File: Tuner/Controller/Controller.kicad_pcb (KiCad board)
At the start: 2 copper layers, 96.8 x 99.3 mm, 173 parts, among them J1 Conn_02x05_Odd_Even, J10 Conn_01x05, J11 Conn_01x01, J12 Conn_01x02, J14 Conn_01x01, J15 Conn_01x02, J16 Conn_01x06, J17 Conn_01x01, J18 Conn_01x01, J19 Conn_01x01, J2 Conn_02x05_Odd_Even, J20 Conn_01x01, J21 Conn_01x01, J23 Conn_01x01, J26 Conn_01x02, J27 Conn_01x02, J28 Conn_01x02, J3 Conn_02x05_Odd_Even, J30 Conn_01x02, J4 Conn_02x05_Odd_Even, J5 Conn_02x05_Odd_Even, J7 Conn_01x02, J8 Conn_01x06, Q1 2N3904, Q2 2N3904, Q3 2N3904, Q4 2N3904, Q5 2N3904, Q6 2N3904, Q7 2N3904, Q8 2N3904, U1 74LS393, U2 74HC14, U3 74HC86, U4 LM350_TO220

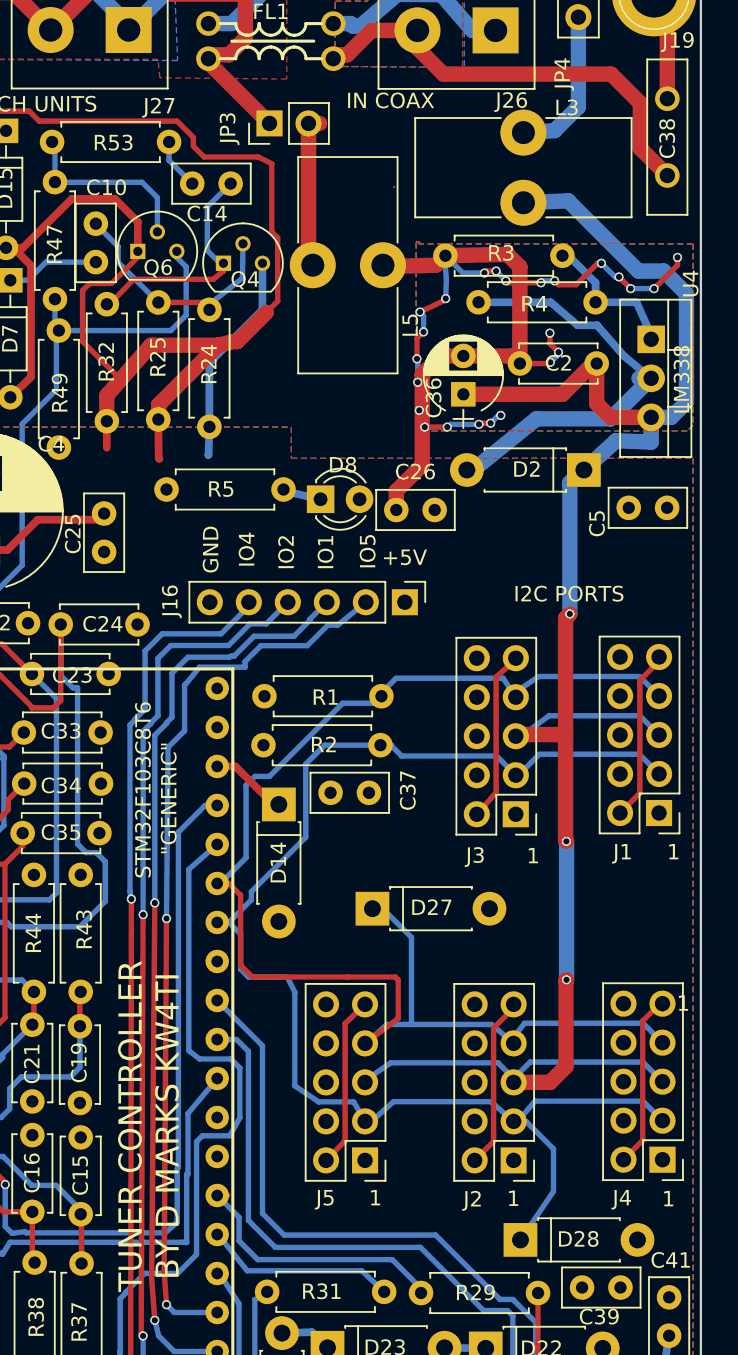
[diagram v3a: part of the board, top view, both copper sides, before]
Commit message: Added HK19F boards
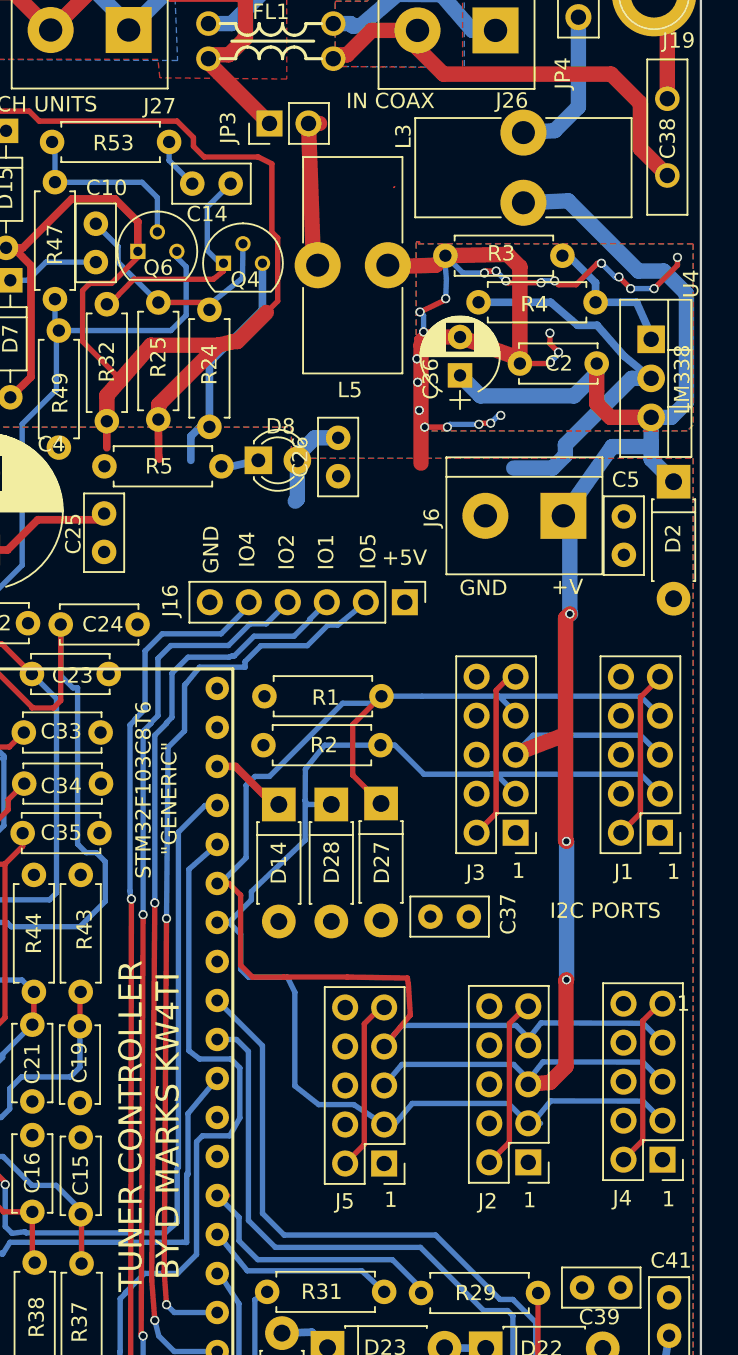
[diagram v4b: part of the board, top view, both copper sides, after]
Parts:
- added J6: Conn_01x02, Connectors_Terminal_Blocks:TerminalBlock_bornier-2_P5.08mm, F.Cu at (143.2, 66.0)
- moved D28 30.9 mm to (128.1, 84.8), turned to 270 degrees
- moved C37 10.4 mm to (137.0, 92.1)
- moved C26 7.85 mm to (128.5, 60.9), turned to 270 degrees
- moved D27 6.87 mm to (131.3, 84.7), turned to 270 degrees
- moved D2 5.89 mm to (150.4, 63.8), turned to 270 degrees
- moved D8 4.78 mm to (123.3, 62.4)
- moved R5 4.32 mm to (120.9, 62.8)
- moved C5 3.08 mm to (147.1, 68.5), turned to 90 degrees
- moved J1 1.29 mm to (149.5, 86.6)
- moved J5 1.26 mm to (131.5, 108.2)
- moved C36 1.25 mm to (136.5, 56.8)
- moved J3 1.21 mm to (140.1, 86.6)
- moved J2 0.96 mm to (140.9, 108.1)
- moved L5 0.32 mm to (127.2, 49.7)
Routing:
- net +5V: track 193.8 -> 199.7 mm
- net I2CSCL: track 91.9 -> 87.5 mm
- net UPWR: track 124.0 -> 127.7 mm
- net GND: track 622.4 -> 620.3 mm

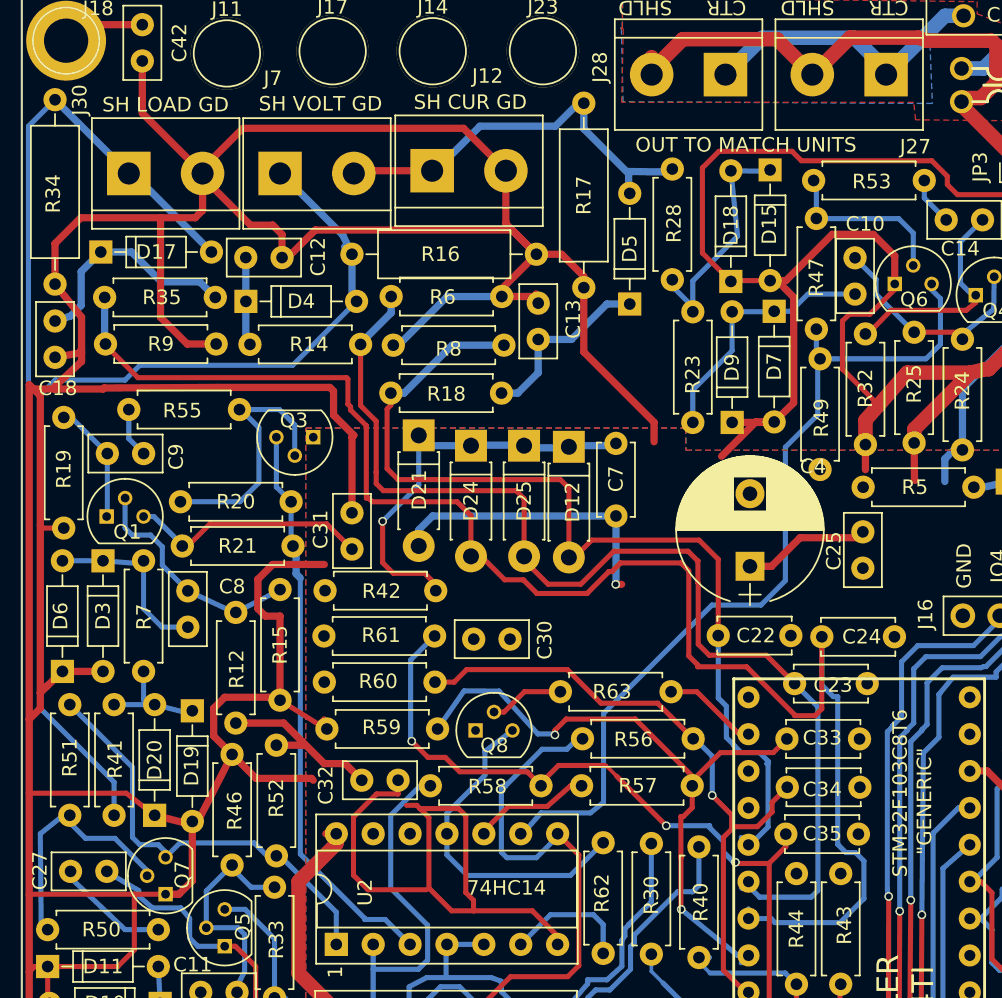
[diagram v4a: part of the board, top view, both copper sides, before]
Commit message: Moved some grounds around
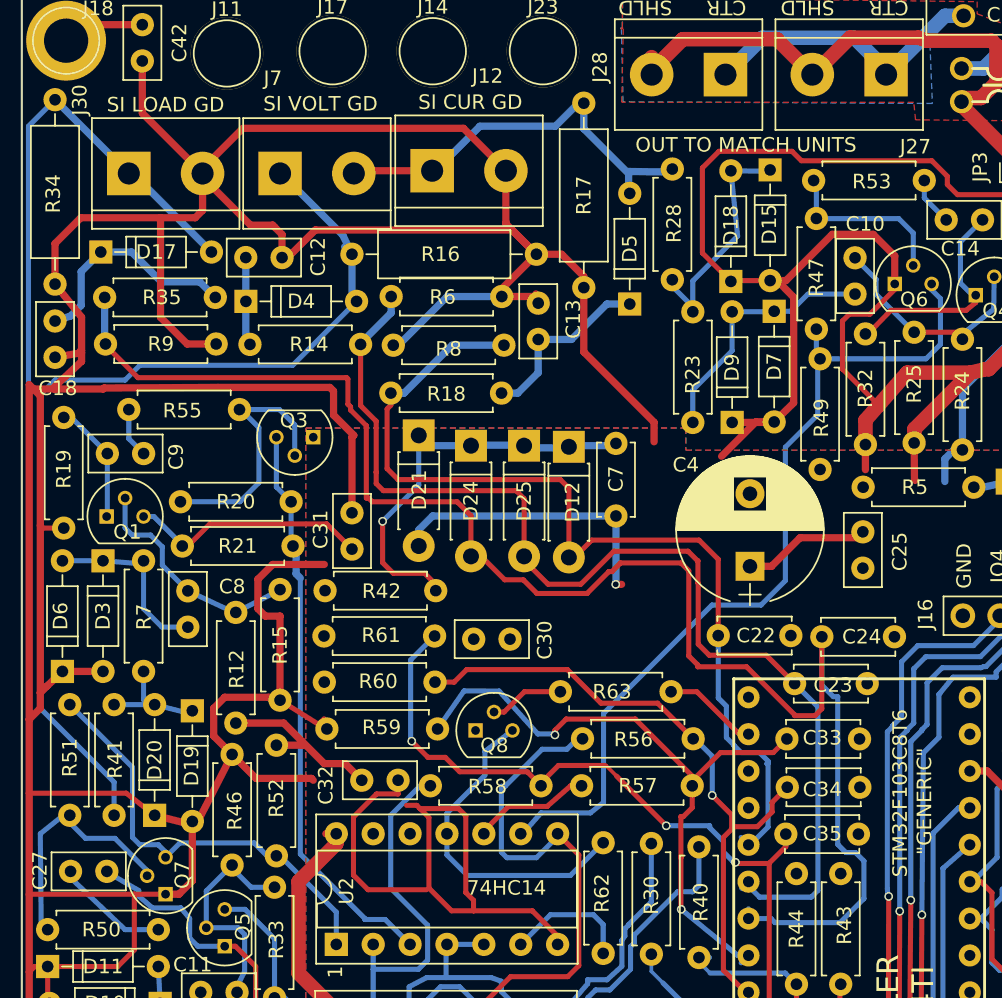
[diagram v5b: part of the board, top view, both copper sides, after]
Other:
- board text added: "SI CUR GD"
- board text added: "SI LOAD GD"
- board text added: "SI VOLT GD"
- board text removed: "SH CUR GD"
- board text removed: "SH LOAD GD"
- board text removed: "SH VOLT GD"
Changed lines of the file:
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@@
     (links 361)
     (no_connects 0)
-    (area 53.127 26.7545 157.029022 130.223619)
+    (area 55.296999 28.880999 152.221001 128.345001)
     (thickness 1.6)
     (drawings 55)
@@
     (descr "CP, Radial series, Radial, pin pitch=5.00mm, , diameter=10mm, Electrolytic Capacitor")
     (tags "CP Radial series Radial pin pitch 5.00mm  diameter 10mm Electrolytic Capacitor")
-    (fp_text reference C4 (at 6.8834 4.3434 180) (layer F.SilkS)
+    (fp_text reference C4 (at 6.985 -4.4196 180) (layer F.SilkS)
       (effects (font (size 1 1) (thickness 0.15)))
     )
@@
     (descr "14-lead though-hole mounted DIP package, row spacing 7.62 mm (300 mils), Socket")
     (tags "THT DIP DIL PDIP 2.54mm 7.62mm 300mil Socket")
-    (fp_text reference U2 (at 3.5814 1.9812 90) (layer F.SilkS)
+    (fp_text reference U2 (at 3.683 0.6985 90) (layer F.SilkS)
       (effects (font (size 1 1) (thickness 0.15)))
     )
@@
     (descr "C, Disc series, Radial, pin pitch=2.50mm, , diameter*width=5*2.5mm^2, Capacitor, http://cdn-reichelt.de/documents/datenblatt/B300/DS_KERKO_TC.pdf")
     (tags "C Disc series Radial pin pitch 2.50mm  diameter 5mm width 2.5mm Capacitor")
-    (fp_text reference C25 (at 1.18618 -1.99898 90) (layer F.SilkS)
+    (fp_text reference C25 (at 1.143 2.54 90) (layer F.SilkS)
       (effects (font (size 1 1) (thickness 0.15)))
     )
@@
     (effects (font (size 1 1) (thickness 0.15)))
   )
-  (gr_text "SH LOAD GD" (at 65.26784 36.41344) (layer F.SilkS)
+  (gr_text "SI LOAD GD" (at 65.26784 36.41344) (layer F.SilkS)
     (effects (font (size 1 1) (thickness 0.15)))
   )
@@
     (effects (font (size 1 1) (thickness 0.15)))
   )
-  (gr_text "SH VOLT GD" (at 75.93584 36.35248) (layer F.SilkS)
+  (gr_text "SI VOLT GD" (at 75.93584 36.35248) (layer F.SilkS)
     (effects (font (size 1 1) (thickness 0.15)))
   )
-  (gr_text "SH CUR GD" (at 86.25078 36.23818) (layer F.SilkS)
+  (gr_text "SI CUR GD" (at 86.25078 36.23818) (layer F.SilkS)
     (effects (font (size 1 1) (thickness 0.15)))
   )

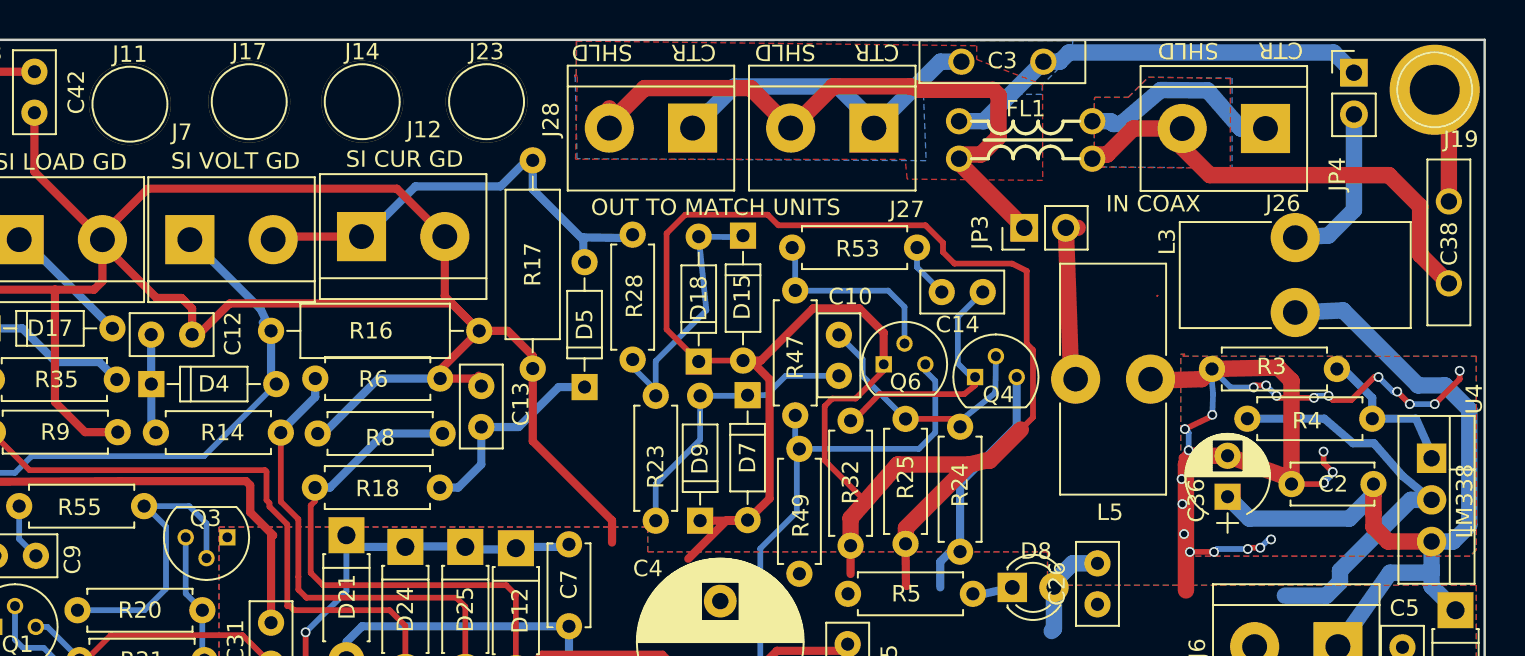
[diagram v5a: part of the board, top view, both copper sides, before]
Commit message: Tandem Match PCB added
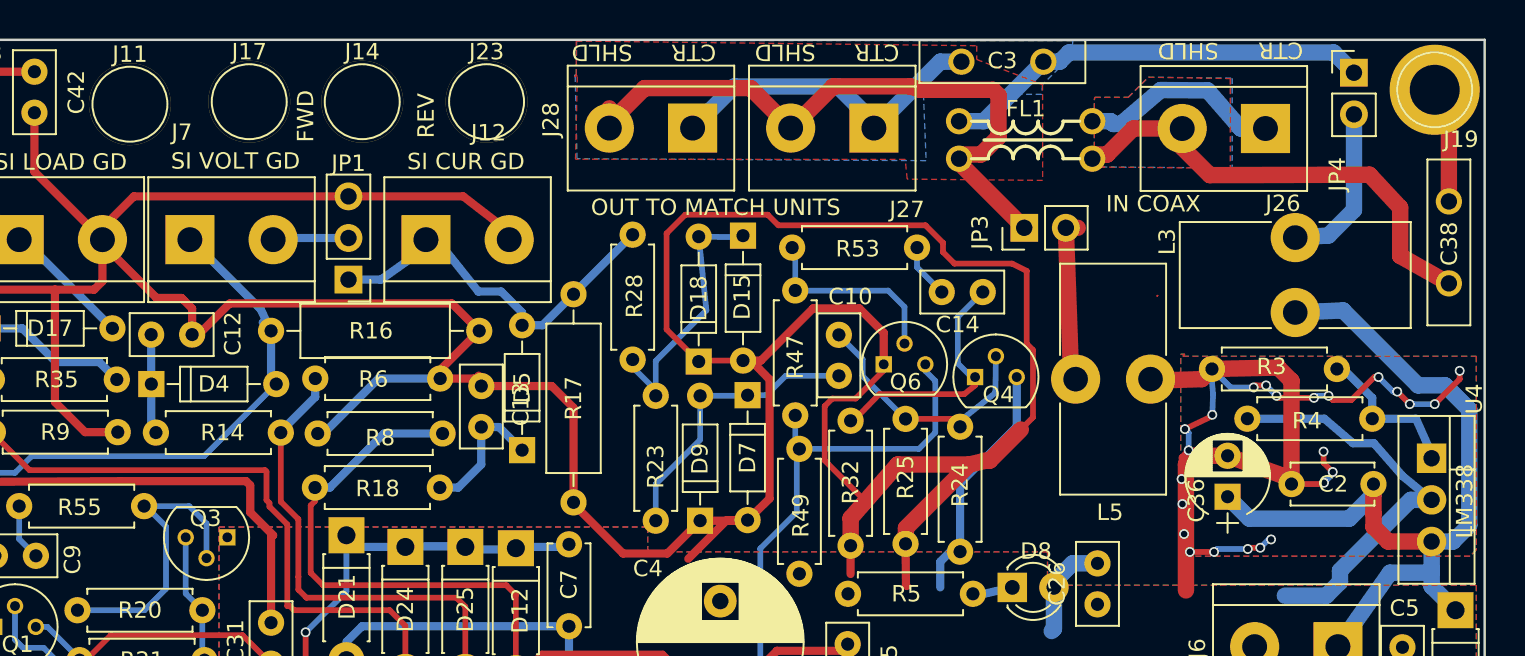
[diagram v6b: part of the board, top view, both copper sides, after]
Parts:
- added JP1: Jumper_NC_Dual, Pin_Headers:Pin_Header_Straight_1x03_Pitch2.54mm, F.Cu at (82.8, 43.6)
- moved R17 8.54 mm to (96.6, 44.5)
- moved D5 5.42 mm to (93.4, 54.0)
- moved J12 3.93 mm to (87.6, 41.1)
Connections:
- J7 pad 2: XRev -> Net-(J7-Pad2)
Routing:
- net Net-(J7-Pad2): track 0.00 -> 4.91 mm
- net XRev: track 28.6 -> 24.3 mm
- net Net-(C13-Pad1): track 13.7 -> 9.43 mm
- net GND: track 620.3 -> 622.5 mm
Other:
- board text added: "FWD"
- board text added: "REV"
